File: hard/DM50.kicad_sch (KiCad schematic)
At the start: 88 parts, among them J2 USB_C_Receptacle_USB2.0_14P, J3 ST-LINK, Q1 MMBT3904, SW1 F1, SW10 SQR, SW11 LOG, SW12 LN, SW13 XEQ, SW14 STO, SW15 RCL, SW16 R, SW17 SIN, SW18 COS, SW19 TAN, SW2 F2, SW20 ENTER, SW21 ENTER, SW22 x<>y, SW23 +/-, SW24 E, SW25 DEL, SW26 UP, SW27 7, SW28 8, SW29 9, SW3 F3, SW30 /, SW31 DOWN, SW32 4, SW33 5, SW34 6, SW35 x, SW36 OPT, SW37 1, SW38 2, SW39 3, SW4 F4, SW40 -, SW41 ON, SW42 0, SW43 ., SW44 R/S, SW45 +, SW46 SW_RESET, SW5 F5, SW6 F6, SW8 E+, SW9 1/x, U1 EA_DOGL128X-6, U2 STM32U535CBT6, U3 W25Q32JVSS, U4 ADP2108AUJ-3.3, U5 USBLC6-2SC6, Y1 HC/49US 8MHz

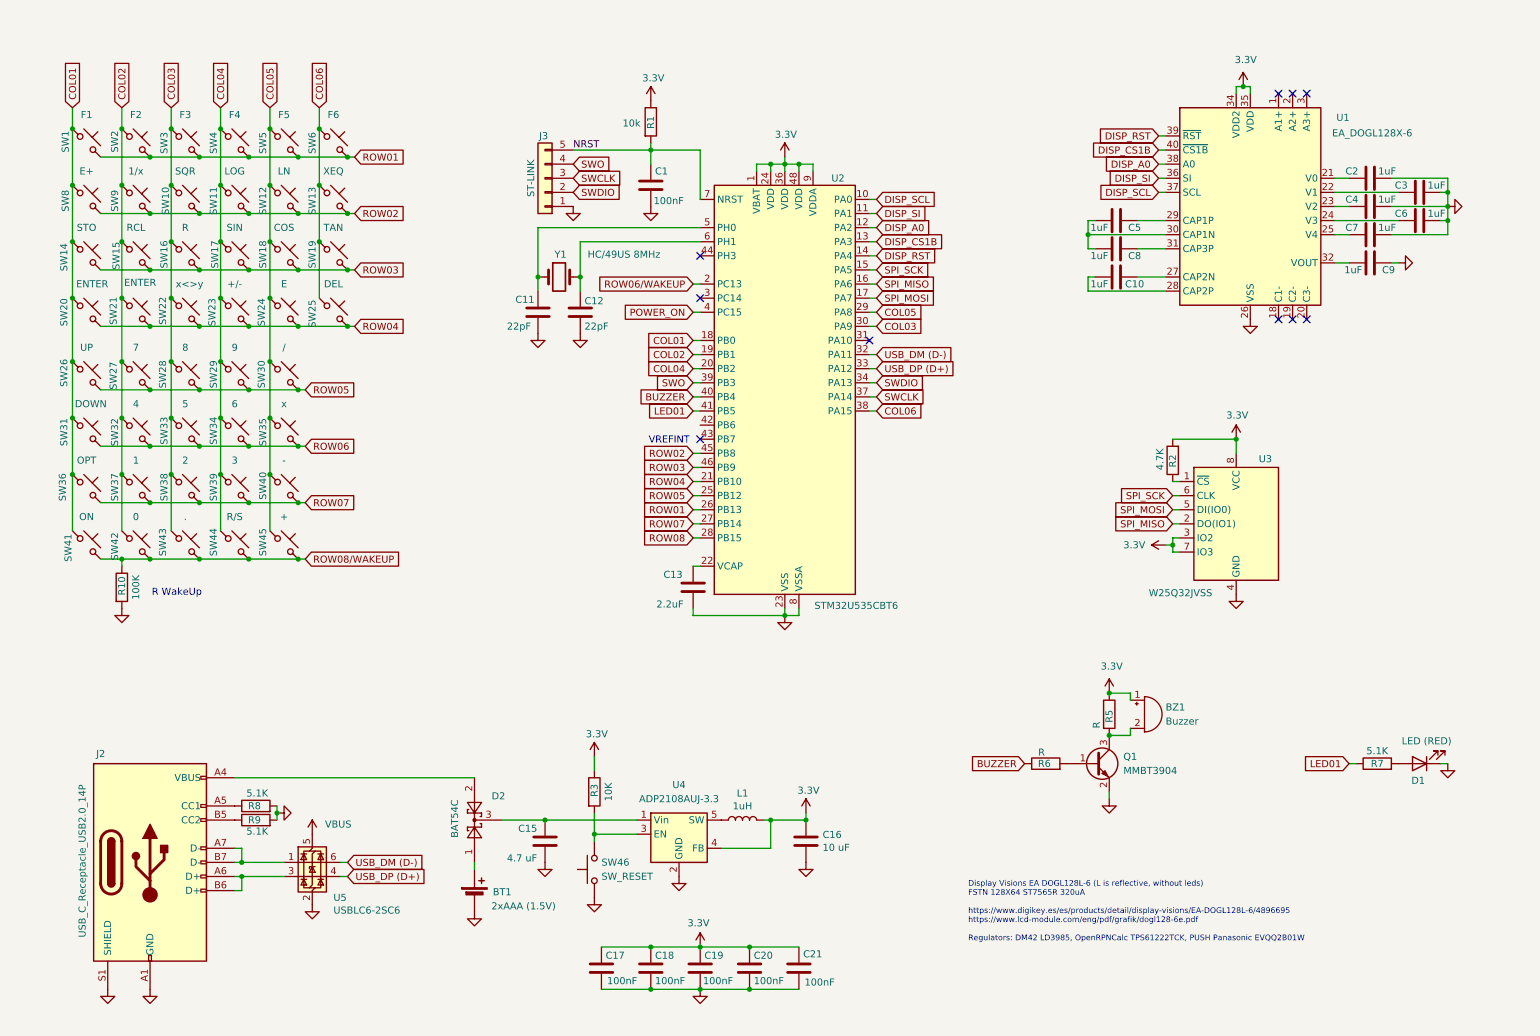
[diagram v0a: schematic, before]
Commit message: Schema updates
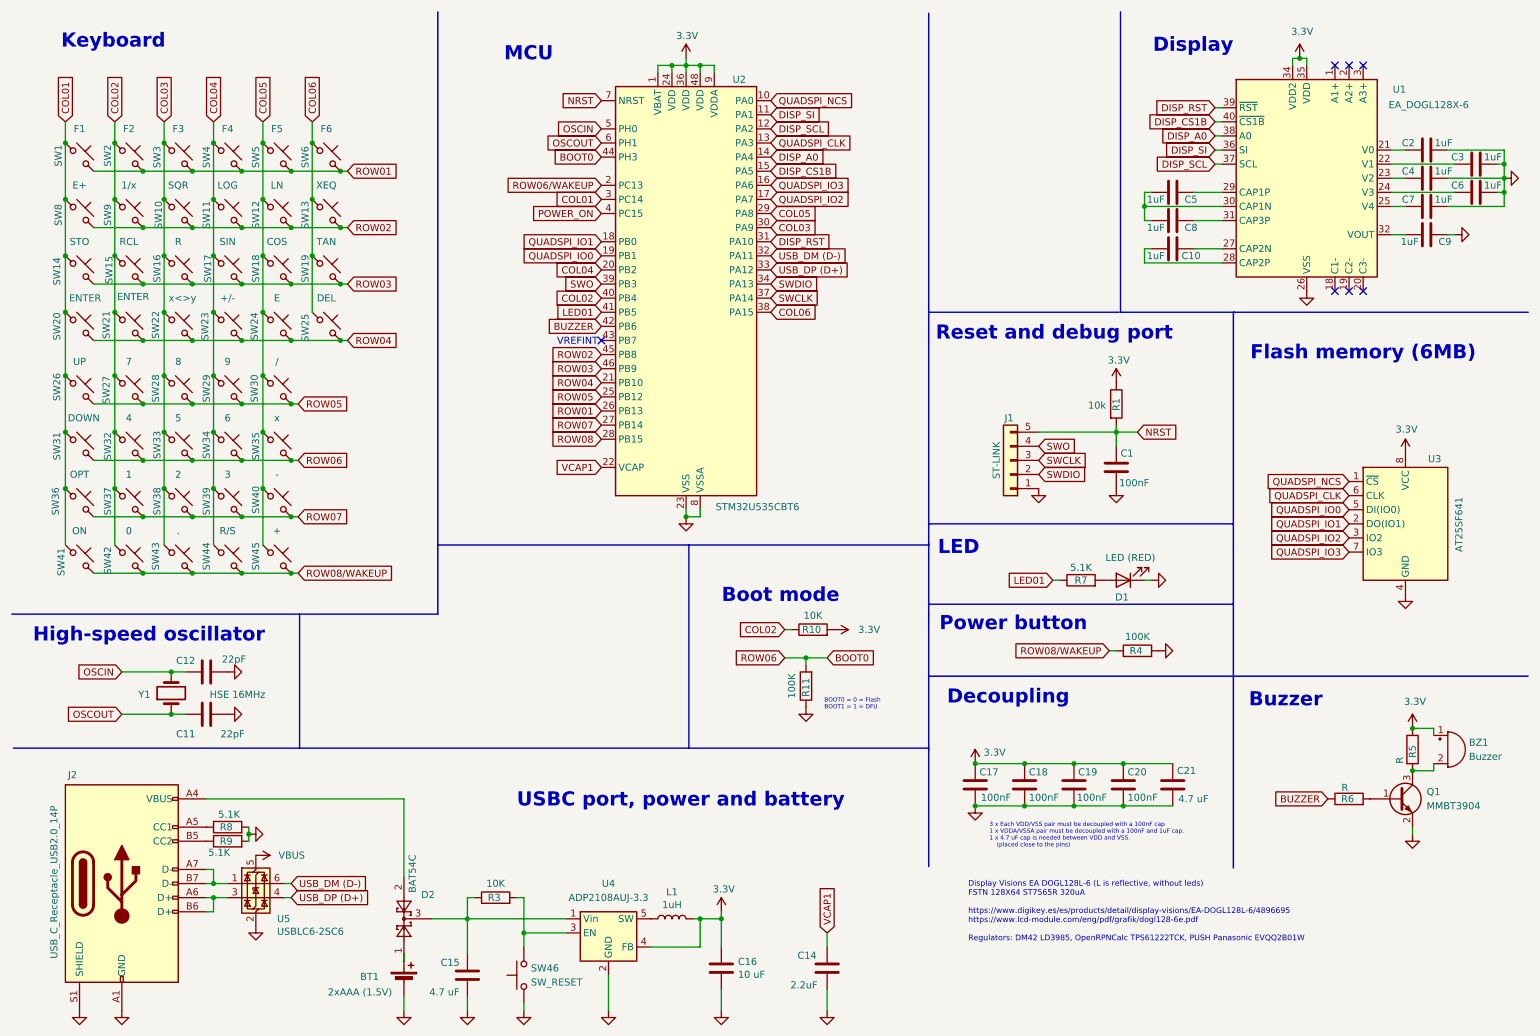
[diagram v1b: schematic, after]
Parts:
- removed C13: 2.2uF, Capacitor_SMD:C_0603_1608Metric, symbol Device:C
- removed J3: ST-LINK, symbol Connector_Generic:Conn_01x05
- removed R2: 4.7K, Resistor_SMD:R_0603_1608Metric, symbol Device:R
- added C14: 2.2uF, Capacitor_SMD:C_0603_1608Metric, symbol Device:C
- added J1: ST-LINK, symbol Connector_Generic:Conn_01x05
- added R11, R4: 100K, Resistor_SMD:R_0603_1608Metric, symbol Device:R
- C21: value 100nF -> 4.7 uF
- R10: value 100K -> 10K
- U3: value W25Q32JVSS -> AT25SF641
- Y1: value HC/49US 8MHz -> HSE 16MHz
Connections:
- net ROW06 is gone; now on net BOOT0: SW31.2, SW32.2, SW33.2, SW34.2, SW35.2
- net 3.3V: now also R10.2; no longer R3.1, U3.3 (IO2), U3.7 (IO3)
- net BUZZER: now also U2.42 (PB6); no longer U2.40 (PB4)
- net COL01: now also U2.3 (PC14); no longer U2.18 (PB0)
- net COL02: now also R10.1, U2.40 (PB4); no longer U2.19 (PB1)
- net DISP_A0: now also U2.14 (PA4); no longer U2.12 (PA2)
- net DISP_CS1B: now also U2.15 (PA5); no longer U2.13 (PA3)
- net DISP_RST: now also U2.31 (PA10); no longer U2.14 (PA4)
- net DISP_SCL: now also U2.12 (PA2); no longer U2.10 (PA0)
- net GND: now also C14.2, J1.1 (Pin_1), R11.1, R4.2; no longer R10.2
- net NRST: now also J1.5 (Pin_5)
- net ROW08/WAKEUP: now also R4.1; no longer R10.1
- net SWCLK: now also J1.3 (Pin_3)
- net SWDIO: now also J1.2 (Pin_2)
- net SWO: now also J1.4 (Pin_4)
- net QUADSPI_NCS: now reaches U3.1 (~{CS})
- net QUADSPI_NCS: now also U2.10 (PA0)
- net VCAP1: now reaches U2.22 (VCAP)
- net VCAP1: now also C14.1
- net BOOT0: now reaches U2.44 (PH3)
- net BOOT0: now also R11.2
- net OSCOUT: now reaches C11.1, Y1.1
- net OSCOUT: now also U2.6 (PH1); no longer U2.5 (PH0)
- net OSCIN: now reaches C12.1, Y1.2
- net OSCIN: now also U2.5 (PH0); no longer U2.6 (PH1)
- net at C15.1, D2.3, U4.1 (Vin): now also R3.1
- net SPI_MISO renamed QUADSPI_IO1
- net QUADSPI_IO1: now also U2.18 (PB0); no longer U2.16 (PA6)
- net SPI_MOSI renamed QUADSPI_IO0
- net QUADSPI_IO0: now also U2.19 (PB1); no longer U2.17 (PA7)
- net SPI_SCK renamed QUADSPI_CLK
- net QUADSPI_CLK: now also U2.13 (PA3); no longer U2.15 (PA5)
- new net QUADSPI_IO2: U2.17 (PA7), U3.3 (IO2)
- new net QUADSPI_IO3: U2.16 (PA6), U3.7 (IO3)
- no-connect marks 10 -> 7
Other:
- note added: "3 x Each VDD/VSS pair must be decoupled with a 100nF cap 1 x VDDA/VSSA pair must be decoupled with a 100nF and 1uF cap. 1 x 4.7 uF cap is needed between VDD and VSS. (placed close to the pins)"
- note added: "BOOT0 = 0 = Flash BOOT1 = 1 = DFU"
- note added: "Boot mode"
- note added: "Buzzer"
- note added: "Decoupling"
- note added: "Display"
- note added: "Flash memory (6MB)"
- note added: "High-speed oscillator"
- note added: "Keyboard"
- note added: "LED"
- note added: "MCU"
- note added: "Power button"
- note added: "Reset and debug port"
- note added: "USBC port, power and battery"
- note removed: "R WakeUp"
- moved on the sheet: BT1, BZ1, C10, C11, C12, C15, C16, C17, C18, C19, C2, C20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

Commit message: Update DM50.kicad_sch
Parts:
- added C13: 100nF, Capacitor_SMD:C_0603_1608Metric, symbol Device:C
- added R12, R2: 1M, Resistor_SMD:R_0603_1608Metric, symbol Device:R
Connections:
- net VBUS is gone; now on an unnamed net: U5.5 (VBUS)
- net DISP_SI: now also U2.43 (PB7); no longer U2.11 (PA1)
- net GND: now also C13.2, R12.1
- net VBAT: now reaches BT1.1 (+), D2.1
- net VBAT: now also R2.2
- net SWCLK renamed SWD_SWCLK
- net SWDIO renamed SWD_SWDIO
- net SWO renamed SWD_SWO
- new net VBAT_SNS: C13.1, R12.2, R2.1, U2.11 (PA1)
- no-connect marks 7 -> 6
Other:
- note added: "Battery voltage measusement"
- note removed: "VREFINT"
- moved on the sheet: J1
